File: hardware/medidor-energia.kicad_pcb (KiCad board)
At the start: 2 copper layers, 150 x 90 mm, 53 parts, among them J1 Bornera 5 V, J2 Jack 3,5 mm de panel (pinza S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, J3 Jack 3,5 mm de panel (pinza S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, J5 Bornera ZMPT, J6 OLED (GND VCC SCL SDA), J7 Reserva ADC1, SW1 Pulsador de panel 12 mm NA, SW2 Pulsador de panel 12 mm NA, U1 ESP32-DevKitC V4 (38 pines)

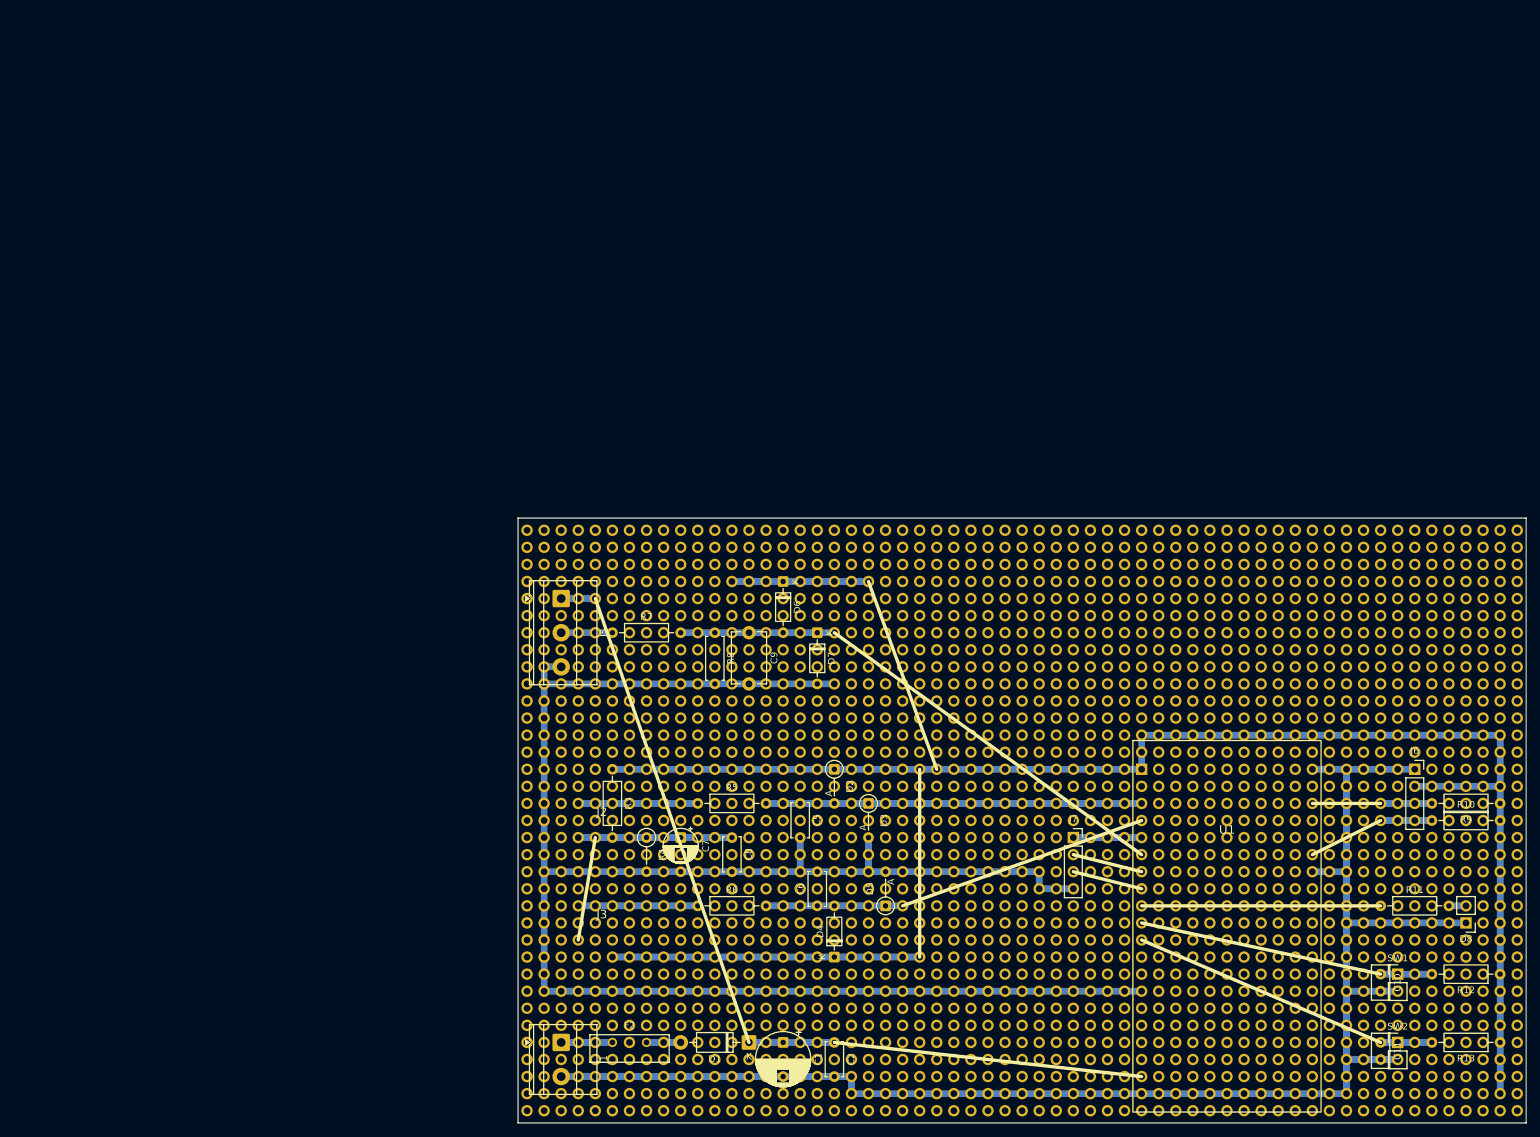
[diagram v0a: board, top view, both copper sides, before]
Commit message: PCB de una cara para fabricar por tóner y gabinete ajustado a ella
- herramientas/generar_pcb.py: PCB de 150 × 90 mm con cobre solo abajo, ruteada con
  Freerouting (4 puentes de alambre), relleno de GND y agujeros M3; DRC sin conexiones
  pendientes ni diferencias con el esquemático
- herramientas/exportar_fabricacion.sh: PDF 1:1 para tóner, Gerber, taladros, guía de
  montaje, lista de puentes, vistas 3D y STEP
- freecad: cables hasta los pads reales (conectores.json), jacks y USB alineados con la PCB,
  tornillos M3, rótulos con tildes y vistas del medidor en Blender
- Documento: sección 7.7 (PCB y alternativa en placa perforada), materiales, cronograma,
  dificultades y anexo; diagrama de bloques con HTTP y la plataforma web
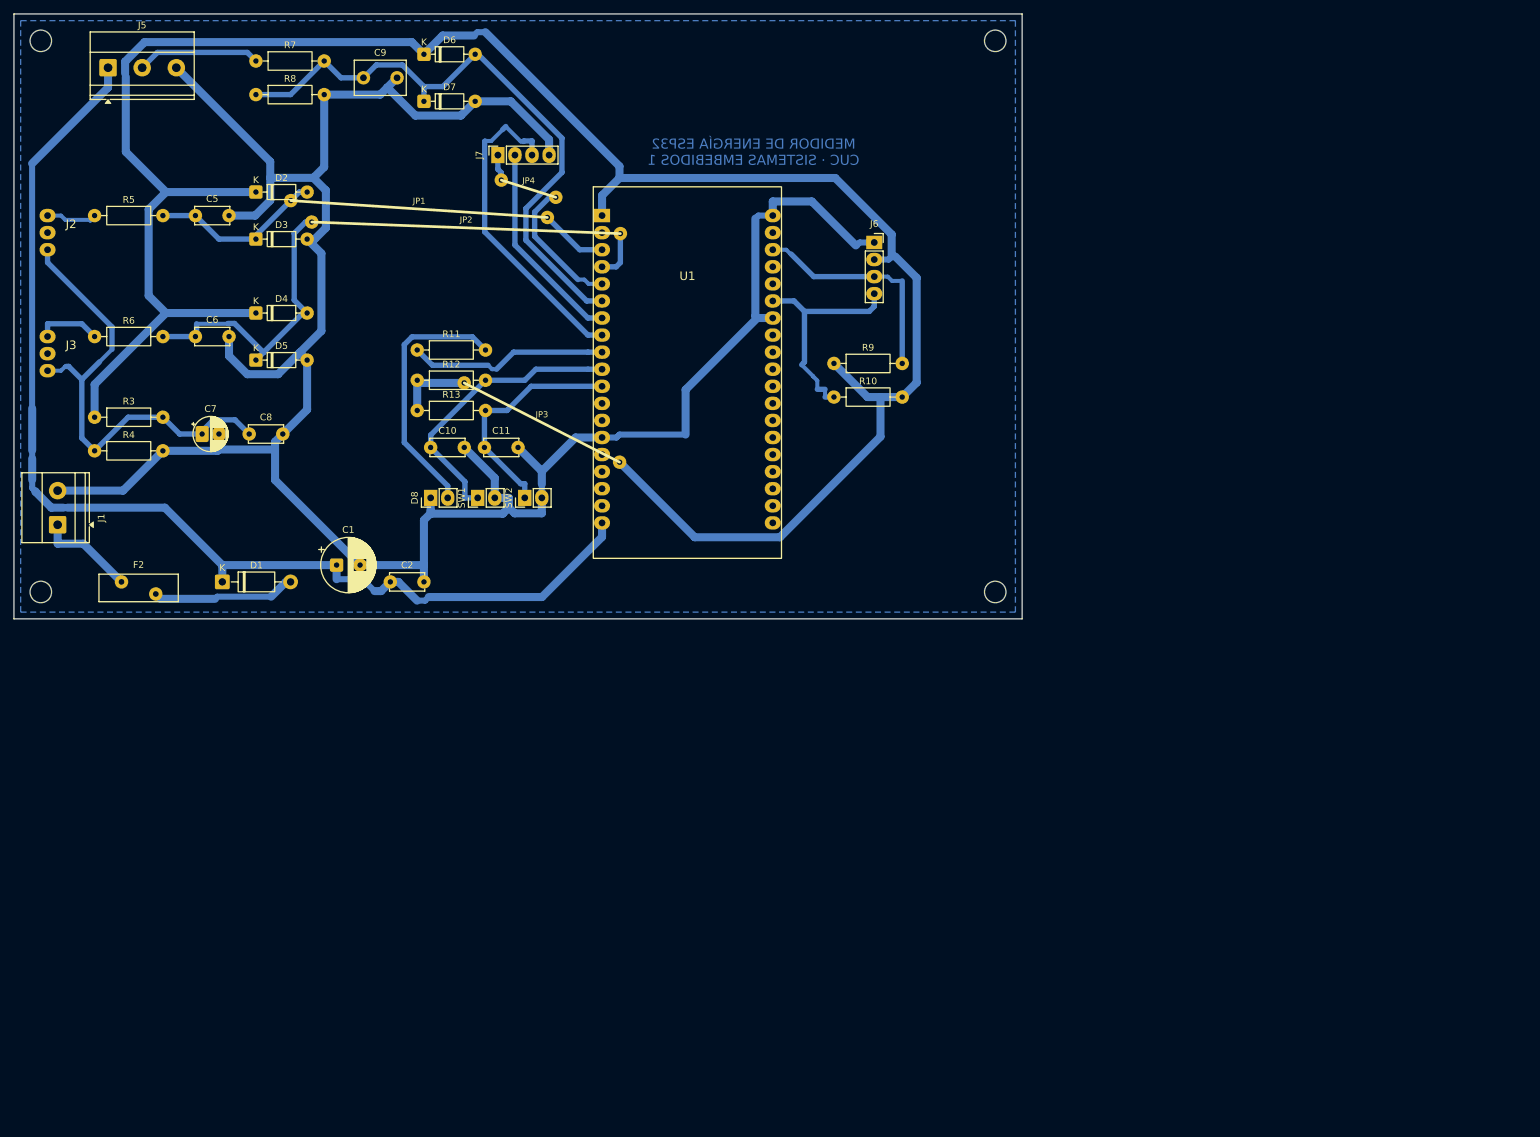
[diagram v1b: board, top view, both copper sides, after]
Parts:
- removed PERF1: Placa perforada 9 × 15 cm, 59 × 35 agujeros, Medidor:Placa_Perforada_59x35
- removed W1: Puente 3V3, Puente_Cable_1
- removed W10: Puente I2C, Puente_Cable_10
- removed W11: Puente I2C, Puente_Cable_11
- removed W12: Puente DIG, Puente_Cable_12
- removed W13: Puente DIG, Puente_Cable_13
- removed W14: Puente DIG, Puente_Cable_14
- removed W2: Puente 3V3, Puente_Cable_2
- removed W3: Puente 5V, Puente_Cable_3
- removed W4: Puente 5V, Puente_Cable_4
- removed W5: Puente VBIAS, Puente_Cable_5
- removed W6: Puente CORR, Puente_Cable_6
- removed W7: Puente TENS, Puente_Cable_7
- removed W8: Puente RES, Puente_Cable_8
- removed W9: Puente RES, Puente_Cable_9
- added H1: MountingHole_3.2mm_M3, MountingHole:MountingHole_3.2mm_M3, F.Cu at (29.0, 29.0)
- added H2: MountingHole_3.2mm_M3, MountingHole:MountingHole_3.2mm_M3, F.Cu at (171.0, 29.0)
- added H3: MountingHole_3.2mm_M3, MountingHole:MountingHole_3.2mm_M3, F.Cu at (29.0, 111.0)
- added H4: MountingHole_3.2mm_M3, MountingHole:MountingHole_3.2mm_M3, F.Cu at (171.0, 111.0)
- added JP1: puente, Medidor:Puente_alambre, F.Cu at (66.2, 52.8)
- added JP2: puente, Medidor:Puente_alambre, F.Cu at (69.3, 56.0)
- added JP3: puente, Medidor:Puente_alambre, F.Cu at (92.0, 79.9)
- added JP4: puente, Medidor:Puente_alambre, F.Cu at (97.5, 49.7)
- C1: footprint Capacitor_THT:CP_Radial_D8.0mm_P5.00mm -> Capacitor_THT:CP_Radial_D8.0mm_P3.50mm
- C10, C11: footprint Capacitor_THT:C_Disc_D5.0mm_W2.5mm_P2.50mm -> Capacitor_THT:C_Disc_D5.0mm_W2.5mm_P5.00mm
- C9: footprint Capacitor_THT:C_Disc_D7.5mm_W5.0mm_P7.50mm -> Capacitor_THT:C_Disc_D7.5mm_W5.0mm_P5.00mm
- D2, D3, D5: footprint Diode_THT:D_DO-35_SOD27_P5.08mm_Vertical_AnodeUp -> Diode_THT:D_DO-35_SOD27_P7.62mm_Horizontal
- R4: footprint Resistor_THT:R_Axial_DIN0207_L6.3mm_D2.5mm_P5.08mm_Vertical -> Resistor_THT:R_Axial_DIN0207_L6.3mm_D2.5mm_P10.16mm_Horizontal
- R8: footprint Resistor_THT:R_Axial_DIN0207_L6.3mm_D2.5mm_P7.62mm_Horizontal -> Resistor_THT:R_Axial_DIN0207_L6.3mm_D2.5mm_P10.16mm_Horizontal
- moved R13 186.5 mm to (85.0, 84.0), turned to 0 degrees
- moved R12 183.8 mm to (85.0, 79.5), turned to 0 degrees
- moved D8 166.5 mm to (87.0, 97.0), turned to 90 degrees
- moved R11 165.5 mm to (85.0, 75.0)
- moved C10 161.6 mm to (87.0, 89.5), turned to 0 degrees
- moved C11 160.0 mm to (95.0, 89.5), turned to 0 degrees
- moved SW1 154.1 mm to (94.0, 97.0), turned to 90 degrees
- moved SW2 153.1 mm to (101.0, 97.0), turned to 90 degrees
- moved J7 132.8 mm to (97.0, 46.0), turned to 90 degrees
- moved D4 128.8 mm to (61.0, 69.5), turned to 0 degrees
- moved C5 125.5 mm to (52.0, 55.0), turned to 0 degrees
- moved C6 125.4 mm to (52.0, 73.0), turned to 0 degrees
- moved R5 125.3 mm to (37.0, 55.0)
- moved D5 124.0 mm to (61.0, 76.5), turned to 0 degrees
- moved D3 123.9 mm to (61.0, 58.5), turned to 0 degrees
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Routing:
- net +5V: track 17.8 -> 169.9 mm
- net GND: track 495.3 -> 367.8 mm
- net /V_ADC: track 22.9 -> 92.6 mm
- net +3V3: track 269.2 -> 335.2 mm
- net /RES_IO33: track 0.00 -> 48.3 mm
- net /VBIAS: track 22.9 -> 70.8 mm
- net Net-(D8-A): track 2.54 -> 38.8 mm
- net /SW1: track 7.62 -> 42.9 mm
- net /CH2_ADC: track 20.3 -> 52.2 mm
- net /RES_IO32: track 0.00 -> 30.8 mm
- net /LED_EST: track 0.00 -> 29.7 mm
- net /SW2: track 7.62 -> 34.7 mm
- net /I2C_SDA: track 7.62 -> 34.3 mm
- net /I2C_SCL: track 7.62 -> 33.5 mm
- net /CH1_ADC: track 55.9 -> 36.2 mm
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- added copper zone on B.Cu, net GND
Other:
- board text added: "MEDIDOR DE ENERGÍA ESP32 CUC · SISTEMAS EMBEBIDOS 1"

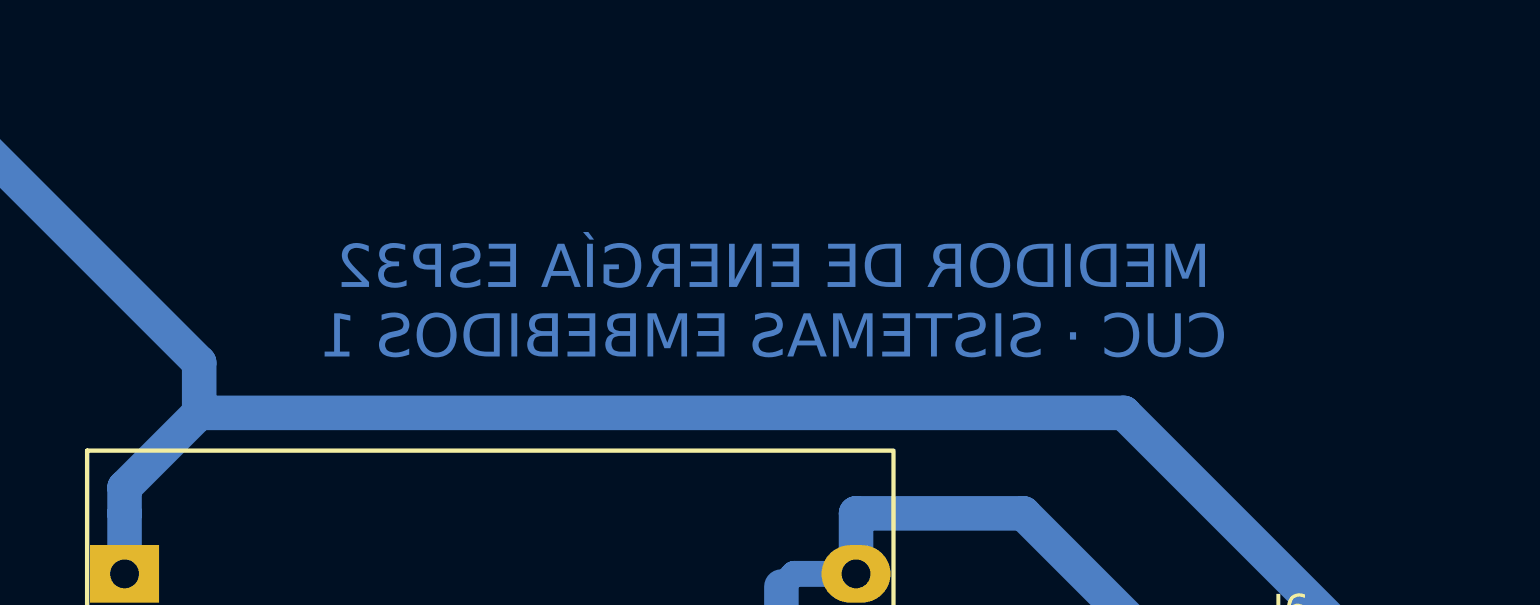
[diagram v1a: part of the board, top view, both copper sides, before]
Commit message: Plataforma sobre Supabase, esquemáticos sin datos personales y redacción revisada
- plataforma: Postgres en Supabase con postgres.js (DATABASE_URL) en lugar de SQLite;
  migración en supabase/migrations con RLS activo; ingesta por lotes en una transacción;
  pnpm db:migrar y .env.ejemplo; pruebas del servicio contra un Postgres de pruebas
- Esquemáticos, PCB y figuras sin nombres ni referencias a asignaturas (revisión B)
- Redacción del documento revisada para un tono más directo y sin exagerar el avance
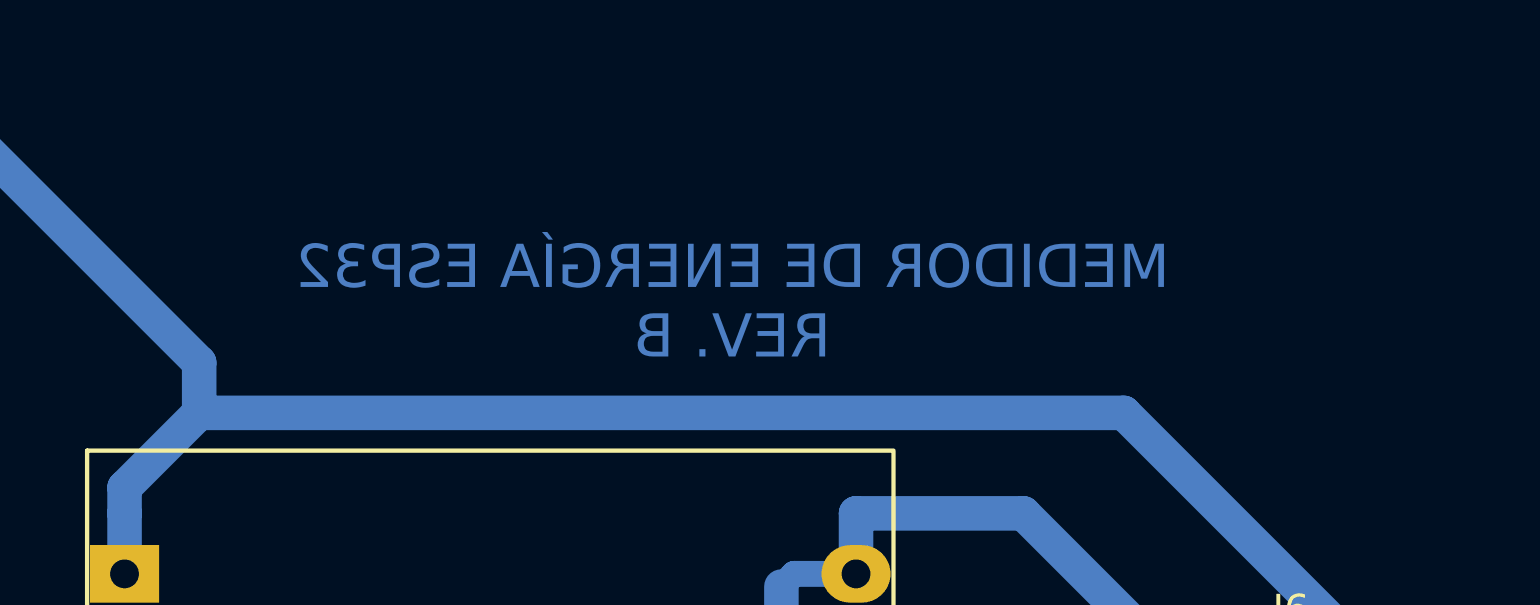
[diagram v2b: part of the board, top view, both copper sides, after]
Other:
- board text added: "MEDIDOR DE ENERGÍA ESP32 REV. B"
- board text removed: "MEDIDOR DE ENERGÍA ESP32 CUC · SISTEMAS EMBEBIDOS 1"

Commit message: LCD Waveshare de 1,9" (ST7789V2, SPI) y modo de demostración para Railway/Render
- Firmware: pantallas en lib/interfaz sobre Adafruit GFX, dibujadas por franjas; energía por hora.
- Las imágenes de las pantallas salen del mismo código compilado en el PC (make -C test pantallas).
- Esquemático: J6 de 8 pines en el orden del DevKitC; se quitan R9 y R10 (pull-up del I2C).
- PCB re-ruteada: 3 puentes, DRC sin conexiones pendientes; placa perforada verificada (25 redes).
- Tapa con ventana para la LCD, diagrama de bloques, README y diagrama de navegación.
- Plataforma: DEMO=1 corre con Postgres en memoria (PGlite) y datos del simulador; Dockerfile,
  railway.json y render.yaml.
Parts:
- removed JP4: puente, Medidor:Puente_alambre
- removed R10, R9: 4,7k, Resistor_THT:R_Axial_DIN0207_L6.3mm_D2.5mm_P10.16mm_Horizontal
- J6: value OLED (GND VCC SCL SDA) -> LCD (VCC GND DIN CS DC BL CLK RST); footprint Connector_PinSocket_2.54mm:PinSocket_1x04_P2.54mm_Vertical -> Connector_PinHeader_2.54mm:PinHeader_1x08_P2.54mm_Vertical
- moved JP3 40.1 mm to (103.6, 41.5)
- moved JP2 22.2 mm to (90.2, 63.6)
- moved JP1 19.5 mm to (68.6, 72.1)
- moved J6 9.92 mm to (149.0, 49.9)
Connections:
- J6 pad 1: GND -> +3V3
- J6 pad 2: +3V3 -> GND
- J6 pad 3: /I2C_SCL -> /LCD_DIN
- J6 pad 4: /I2C_SDA -> /LCD_CS
- JP1 pad 1: /CH1_ADC -> /CH2_ADC
- JP2 pad 1: /CH2_ADC -> /CH1_ADC
- JP3 pad 1: +3V3 -> /V_ADC
- U1 pad 21: unconnected-(U1-IO23-Pad21) -> /LCD_DIN
- U1 pad 22: /I2C_SCL -> /LCD_CS
- U1 pad 25: /I2C_SDA -> /LCD_DC
- U1 pad 27: unconnected-(U1-IO19-Pad27) -> /LCD_BL
- U1 pad 28: unconnected-(U1-IO18-Pad28) -> /LCD_CLK
- U1 pad 32: unconnected-(U1-IO4-Pad32) -> /LCD_RST
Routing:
- net /CH1_ADC: track 36.2 -> 91.1 mm
- net GND: track 367.8 -> 416.5 mm
- net /I2C_SDA: track 34.3 -> 0.00 mm
- net /I2C_SCL: track 33.5 -> 0.00 mm
- net /LCD_RST: track 0.00 -> 23.6 mm
- net /LCD_BL: track 0.00 -> 17.3 mm
- net /LCD_CLK: track 0.00 -> 16.4 mm
- net /LCD_DC: track 0.00 -> 15.7 mm
- net +3V3: track 335.2 -> 320.8 mm
- net /V_ADC: track 92.6 -> 78.8 mm
- net /LCD_DIN: track 0.00 -> 12.2 mm
- net /LCD_CS: track 0.00 -> 12.2 mm
- net /RES_IO34: track 24.6 -> 35.7 mm
- net Net-(D8-A): track 38.8 -> 28.0 mm
- net /RES_IO32: track 30.8 -> 40.4 mm
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
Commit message: Puntos de prueba TP1–TP9 y LED de alimentación en la PCB
- Lazos para la punta del osciloscopio en +5V, +3V3, VBIAS, CH1_ADC, CH2_ADC, ZMPT_OUT y V_ADC,
  y dos de GND; la serigrafía rotula la red de cada uno.
- D9 (+5 V, R14 1 kΩ) y D10 (+3,3 V, R15 470 Ω).
- PCB re-ruteada con 3 puentes; DRC sin errores ni conexiones pendientes; placa perforada con 27 redes.
- README: tabla de valores esperados en cada punto y verificación antes de energizar con los TP.
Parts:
- added D10: LED verde 3 mm, LED_THT:LED_D3.0mm, F.Cu at (139.0, 33.0)
- added D9: LED rojo 3 mm, LED_THT:LED_D3.0mm, F.Cu at (95.0, 104.0)
- added R14: 1k, Resistor_THT:R_Axial_DIN0207_L6.3mm_D2.5mm_P10.16mm_Horizontal, F.Cu at (81.0, 104.0)
- added R15: 470, Resistor_THT:R_Axial_DIN0207_L6.3mm_D2.5mm_P10.16mm_Horizontal, F.Cu at (125.0, 33.0)
- added TP1: +5V, TestPoint:TestPoint_Loop_D2.50mm_Drill1.0mm, F.Cu at (91.0, 111.0)
- added TP2: +3V3, TestPoint:TestPoint_Loop_D2.50mm_Drill1.0mm, F.Cu at (101.0, 40.0)
- added TP3: VBIAS, TestPoint:TestPoint_Loop_D2.50mm_Drill1.0mm, F.Cu at (69.0, 87.5)
- added TP4: CH1_ADC, TestPoint:TestPoint_Loop_D2.50mm_Drill1.0mm, F.Cu at (72.0, 55.0)
- added TP5: CH2_ADC, TestPoint:TestPoint_Loop_D2.50mm_Drill1.0mm, F.Cu at (72.0, 73.0)
- added TP6: ZMPT_OUT, TestPoint:TestPoint_Loop_D2.50mm_Drill1.0mm, F.Cu at (55.0, 44.0)
- added TP7: V_ADC, TestPoint:TestPoint_Loop_D2.50mm_Drill1.0mm, F.Cu at (97.0, 34.5)
- added TP8: GND, TestPoint:TestPoint_Loop_D2.50mm_Drill1.0mm, F.Cu at (72.0, 95.0)
- added TP9: GND, TestPoint:TestPoint_Loop_D2.50mm_Drill1.0mm, F.Cu at (97.0, 111.0)
- moved JP1 36.5 mm to (34.2, 84.4)
- moved JP2 11.3 mm to (80.7, 69.7)
- moved JP3 4.98 mm to (108.0, 43.8)
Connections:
- JP1 pad 1: /CH2_ADC -> +5V
- JP2 pad 1: /CH1_ADC -> /CH2_ADC
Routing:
- net GND: track 416.5 -> 463.1 mm
- net /SW1: track 42.1 -> 68.8 mm
- net +5V: track 169.9 -> 151.5 mm
- net /ZMPT_OUT: track 18.4 -> 33.9 mm
- net /CH2_ADC: track 57.9 -> 73.4 mm
- net +3V3: track 320.8 -> 308.6 mm
- net /VBIAS: track 69.0 -> 79.7 mm
- net Net-(D10-A): track 0.00 -> 9.35 mm
- net Net-(D9-A): track 0.00 -> 9.35 mm
- net /V_ADC: track 78.8 -> 71.3 mm
- net Net-(D8-A): track 28.0 -> 34.7 mm
- net /CH1_ADC: track 91.1 -> 94.3 mm
- net /RES_IO33: track 42.5 -> 44.8 mm
- net /RES_IO32: track 40.4 -> 42.6 mm
- net /RES_IO34: track 35.7 -> 37.8 mm
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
